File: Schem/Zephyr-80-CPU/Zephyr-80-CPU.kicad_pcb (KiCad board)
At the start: 6 copper layers, 160 x 64.4 mm, 23 parts, among them J1 pBITzBus, U1 AS7C4096A-12TCN, U2 ATF22V10C-10PU, U3 Z084000xP, U4 SST39SF040-70-4C-PHE, U5 ATF22V10C-10PU, U6 SN74HC273DWR, U7 SN74HC244DWR, Y1 ECS-2100AX-100

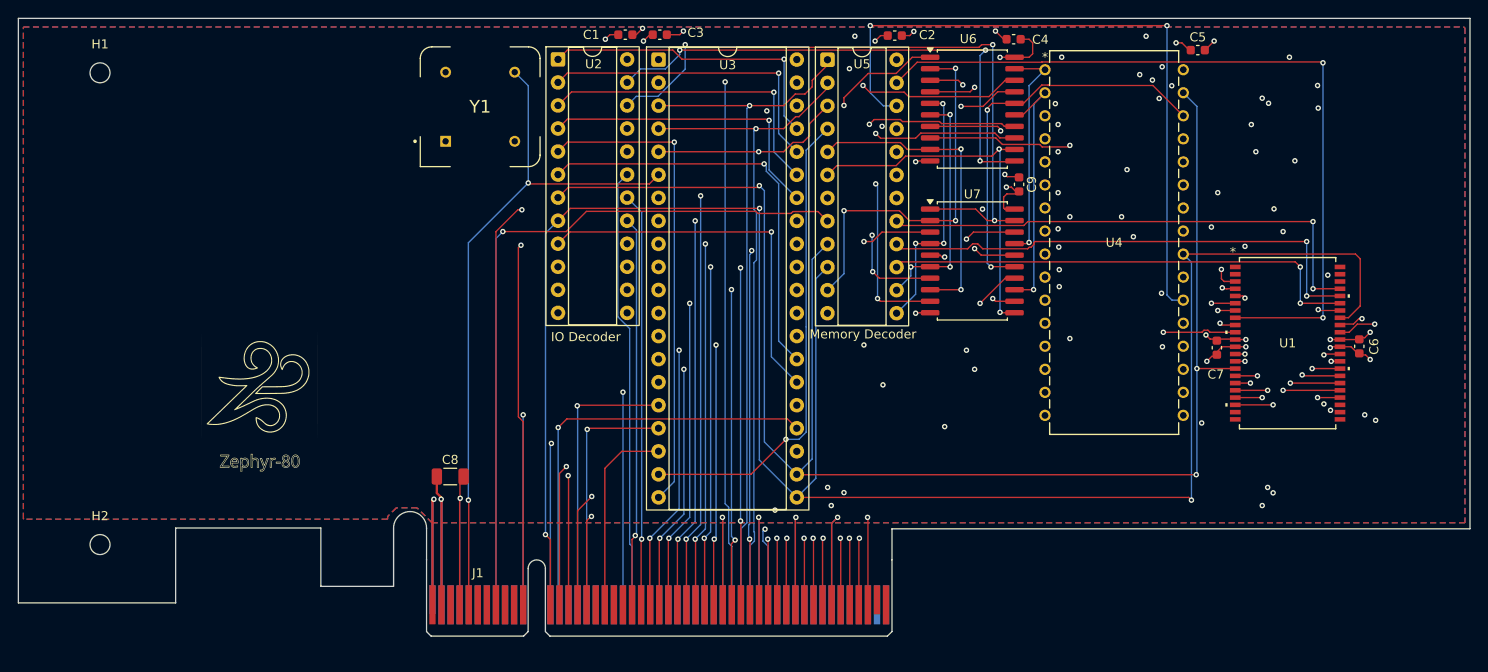
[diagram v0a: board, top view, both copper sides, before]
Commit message: Moved to the DIN Connector
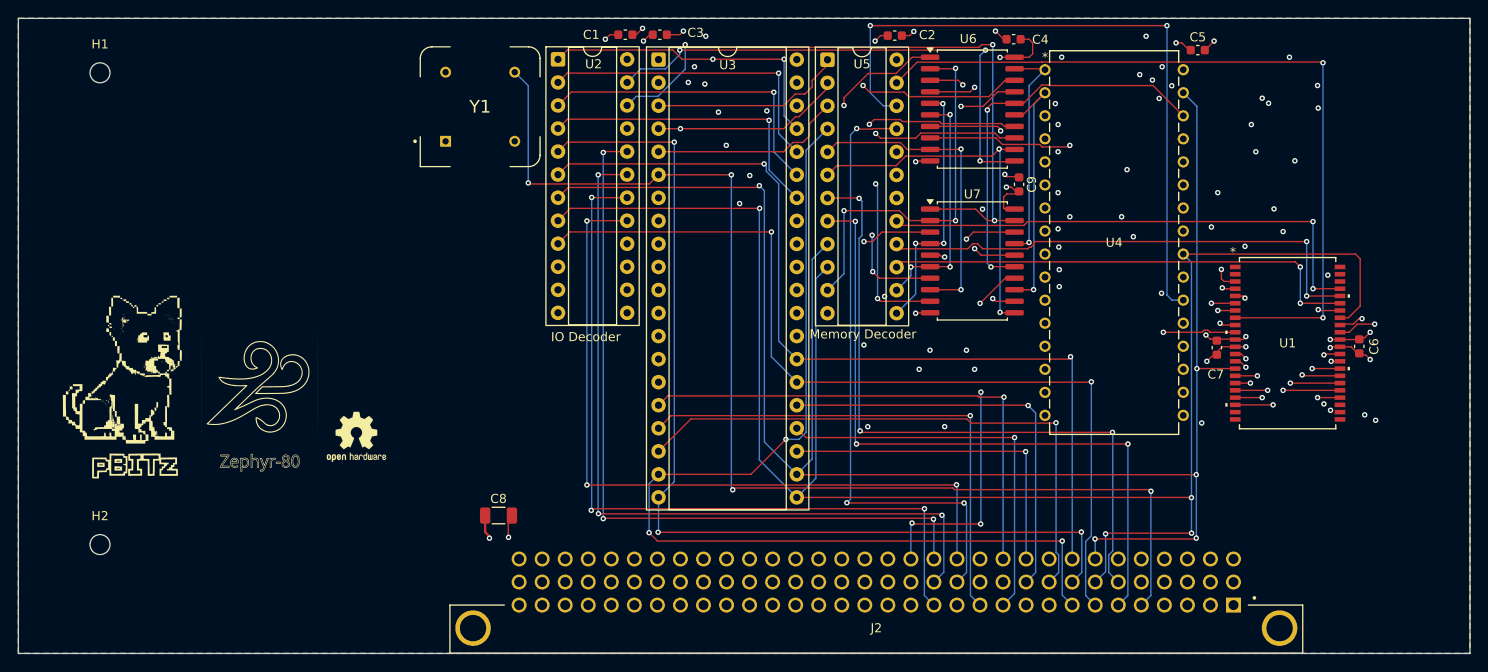
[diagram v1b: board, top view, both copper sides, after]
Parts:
- removed J1: pBITzBus, Connector_PCBEdge:BUS_PCIexpress_x8
- removed the REF** at (106.6, 96.6)
- added J2: ~, Footprints:AMPHENOL_86093967113T55F1LF, F.Cu at (176.9, 118.4)
- added REF**: OSHW-Logo2_7.3x6mm_SilkScreen, Symbol:OSHW-Logo2_7.3x6mm_SilkScreen, F.Cu at (119.6, 97.3)
- G***: moved to F.Cu
- moved G*** 24.1 mm to (95.2, 90.5), turned to 0 degrees
- moved C8 6.85 mm to (135.3, 106.0)
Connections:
- U2 pad 20: unconnected-(U2-IO20-Pad20) -> /CPU and Address Decoding/CS_SEL3
- U4 pad 13: /CPU and Address Decoding/D2 -> /CPU and Address Decoding/D0
- U4 pad 15: /CPU and Address Decoding/D0 -> /CPU and Address Decoding/D2
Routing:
- net GND: track 135.8 -> 25.0 mm, vias 18 -> 13
- net /CPU and Address Decoding/CS_SEL3: track 0.00 -> 84.0 mm, vias 0 -> 3
- net /CPU and Address Decoding/CLK_10M: track 76.9 -> 129.8 mm, vias 2 -> 4
- net +5V: track 76.5 -> 30.0 mm, vias 12 -> 11
- net /CPU and Address Decoding/~{HALT}: track 21.7 -> 63.6 mm, vias 0 -> 1
- net /CPU and Address Decoding/CS_SEL1: track 45.6 -> 86.3 mm, vias 1 -> 3
- net /CPU and Address Decoding/CS_SEL0: track 43.0 -> 82.5 mm, vias 1 -> 3
- net /CPU and Address Decoding/CS_SEL2: track 48.5 -> 86.4 mm, vias 0 -> 3
- net /CPU and Address Decoding/~{IORQ}: track 73.1 -> 109.6 mm, vias 2 -> 3
- net /CPU and Address Decoding/~{MREQ}: track 76.9 -> 112.9 mm, vias 2 -> 3
- net /CPU and Address Decoding/~{NMI}: track 27.3 -> 56.3 mm
- net /CPU and Address Decoding/~{INT}: track 30.9 -> 56.4 mm
- net /CPU and Address Decoding/~{RD}: track 225.1 -> 200.8 mm, vias 3 -> 4
- net /CPU and Address Decoding/~{WR}: track 215.5 -> 194.5 mm, vias 4 -> 5
- net /CPU and Address Decoding/A7: track 202.8 -> 188.4 mm, vias 7 -> 5
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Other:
- board size 160 x 64.4 mm -> 160 x 70 mm

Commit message: updated parts #s
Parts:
- removed REF**: OSHW-Logo2_7.3x6mm_SilkScreen, Symbol:OSHW-Logo2_7.3x6mm_SilkScreen

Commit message: Map ROM bits D5-D7 to the PLD to qualify RAM addresses
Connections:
- U5 pad 18: unconnected-(U5-IO18-Pad18) -> /CPU and Address Decoding/ROM_A16
- U5 pad 19: unconnected-(U5-IO19-Pad19) -> /CPU and Address Decoding/ROM_A17
- U5 pad 20: unconnected-(U5-IO20-Pad20) -> /CPU and Address Decoding/ROM_A18
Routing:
- net /CPU and Address Decoding/ROM_A18: track 24.8 -> 45.0 mm, vias 1 -> 4
- net /CPU and Address Decoding/ROM_A16: track 28.7 -> 44.2 mm, vias 1 -> 2
- net /CPU and Address Decoding/ROM_A17: track 44.3 -> 54.3 mm, vias 2 -> 3
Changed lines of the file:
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@@
 			(layers "*.Cu" "*.Mask")
 			(remove_unused_layers no)
-			(net "unconnected-(U5-IO18-Pad18)")
+			(net "/CPU and Address Decoding/ROM_A16")
 			(pinfunction "IO18_18")
-			(pintype "bidirectional+no_connect")
+			(pintype "bidirectional")
 		)
 		(pad "19" thru_hole circle
@@
 			(layers "*.Cu" "*.Mask")
 			(remove_unused_layers no)
-			(net "unconnected-(U5-IO19-Pad19)")
+			(net "/CPU and Address Decoding/ROM_A17")
 			(pinfunction "IO19_19")
-			(pintype "bidirectional+no_connect")
+			(pintype "bidirectional")
 		)
 		(pad "20" thru_hole circle
@@
 			(layers "*.Cu" "*.Mask")
 			(remove_unused_layers no)
-			(net "unconnected-(U5-IO20-Pad20)")
+			(net "/CPU and Address Decoding/ROM_A18")
 			(pinfunction "IO20_20")
-			(pintype "bidirectional+no_connect")
+			(pintype "bidirectional")
 		)
 		(pad "21" thru_hole circle
@@
 	)
 	(via
+		(at 194.6 70.97)
+		(size 0.6)
+		(drill 0.3)
+		(layers "F.Cu" "B.Cu")
+		(net "/CPU and Address Decoding/ROM_A16")
+	)
+	(via
 		(at 194.25 81.12)
 		(size 0.6)
@@
 	)
 	(segment
-		(start 194.2796 60.6504)
-		(end 194.2796 81.0904)
+		(start 195.51 59.42)
+		(end 194.6 60.33)
 		(width 0.1524)
 		(layer "B.Cu")
@@
 	)
 	(segment
-		(start 195.51 59.42)
-		(end 194.2796 60.6504)
+		(start 194.6 60.33)
+		(end 194.6 70.97)
+		(width 0.1524)
+		(layer "B.Cu")
+		(net "/CPU and Address Decoding/ROM_A16")
+	)
+	(segment
+		(start 194.6 70.97)
+		(end 194.6 80.77)
 		(width 0.1524)
 		(layer "B.Cu")
@@
 	)
 	(segment
-		(start 194.2796 81.0904)
+		(start 194.6 80.77)
 		(end 194.25 81.12)
 		(width 0.1524)
@@
 	)
 	(segment
+		(start 194.6 70.97)
+		(end 194.55 71.02)
+		(width 0.1524)
+		(layer "In3.Cu")
+		(net "/CPU and Address Decoding/ROM_A16")
+	)
+	(segment
+		(start 194.55 71.02)
+		(end 179.15 71.02)
+		(width 0.1524)
+		(layer "In3.Cu")
+		(net "/CPU and Address Decoding/ROM_A16")
+	)
+	(segment
 		(start 207.41 58.62)
 		(end 210.75 61.96)
@@
 	)
 	(segment
+		(start 189.14 68.48)
+		(end 179.15 68.48)
+		(width 0.1524)
+		(layer "F.Cu")
+		(net "/CPU and Address Decoding/ROM_A17")
+	)
+	(segment
 		(start 189.58 78.59)
 		(end 189.55 78.62)
@@
 		(net "/CPU and Address Decoding/ROM_A17")
 	)
+	(segment
+		(start 189.15 68.47)
+		(end 189.14 68.48)
+		(width 0.1524)
+		(layer "F.Cu")
+		(net "/CPU and Address Decoding/ROM_A17")
+	)
 	(via
 		(at 189.15 61.32)
@@
 		(net "/CPU and Address Decoding/ROM_A17")
 	)
+	(via
+		(at 189.15 68.47)
+		(size 0.6)
+		(drill 0.3)
+		(layers "F.Cu" "B.Cu")
+		(net "/CPU and Address Decoding/ROM_A17")
+	)
 	(segment
-		(start 189.15 61.32)
+		(start 189.15 68.47)
 		(end 189.15 78.22)
 		(width 0.1524)
@@
 	)
 	(segment
+		(start 189.15 61.32)
+		(end 189.15 68.47)
+		(width 0.1524)
+		(layer "B.Cu")
+		(net "/CPU and Address Decoding/ROM_A17")
+	)
+	(segment
 		(start 189.15 78.22)
 		(end 189.55 78.62)
@@
 	)
 	(segment
+		(start 187.35 56.72)
+		(end 187.405 56.775)
+		(width 0.1524)
+		(layer "F.Cu")
+		(net "/CPU and Address Decoding/ROM_A18")
+	)
+	(segment
 		(start 193.75 75.92)
 		(end 193.62 76.05)
@@
 	)
 	(segment
+		(start 187.405 56.775)
+		(end 192.15 56.775)
+		(width 0.1524)
+		(layer "F.Cu")
+		(net "/CPU and Address Decoding/ROM_A18")
+	)
+	(segment
 		(start 193.62 76.05)
 		(end 192.15 76.05)
@@
 	)
 	(via
+		(at 181.35 61.22)
+		(size 0.6)
+		(drill 0.3)
+		(layers "F.Cu" "B.Cu")
+		(net "/CPU and Address Decoding/ROM_A18")
+	)
+	(via
 		(at 193.75 75.92)
 		(size 0.6)
@@
 		(net "/CPU and Address Decoding/ROM_A18")
 	)
+	(via
+		(at 185.1214 60.97)
+		(size 0.6)
+		(drill 0.3)
+		(layers "F.Cu" "B.Cu")
+		(net "/CPU and Address Decoding/ROM_A18")
+	)
+	(via
+		(at 187.35 56.72)
+		(size 0.6)
+		(drill 0.3)
+		(layers "F.Cu" "B.Cu")
+		(net "/CPU and Address Decoding/ROM_A18")
+	)
+	(segment
+		(start 180.38 65.94)
+		(end 179.15 65.94)
+		(width 0.1524)
+		(layer "B.Cu")
+		(net "/CPU and Address Decoding/ROM_A18")
+	)
 	(segment
 		(start 193.75 58.64)
@@
 	)
 	(segment
+		(start 181.35 64.97)
+		(end 180.38 65.94)
+		(width 0.1524)
+		(layer "B.Cu")
+		(net "/CPU and Address Decoding/ROM_A18")
+	)
+	(segment
+		(start 181.35 61.22)
+		(end 181.35 64.97)
+		(width 0.1524)
+		(layer "B.Cu")
+		(net "/CPU and Address Decoding/ROM_A18")
+	)
+	(segment
 		(start 195.51 56.88)
 		(end 193.75 58.64)
@@
 		(net "/CPU and Address Decoding/ROM_A18")
 	)
+	(segment
+		(start 185.1214 60.97)
+		(end 184.8714 61.22)
+		(width 0.1524)
+		(layer "In3.Cu")
+		(net "/CPU and Address Decoding/ROM_A18")
+	)
+	(segment
+		(start 184.8714 61.22)
+		(end 181.35 61.22)
+		(width 0.1524)
+		(layer "In3.Cu")
+		(net "/CPU and Address Decoding/ROM_A18")
+	)
+	(segment
+		(start 187.35 56.72)
+		(end 185.1214 58.9486)
+		(width 0.1524)
+		(layer "In4.Cu")
+		(net "/CPU and Address Decoding/ROM_A18")
+	)
+	(segment
+		(start 185.1214 58.9486)
+		(end 185.1214 60.97)
+		(width 0.1524)
+		(layer "In4.Cu")
+		(net "/CPU and Address Decoding/ROM_A18")
+	)
